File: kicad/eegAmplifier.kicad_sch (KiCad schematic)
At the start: 28 parts

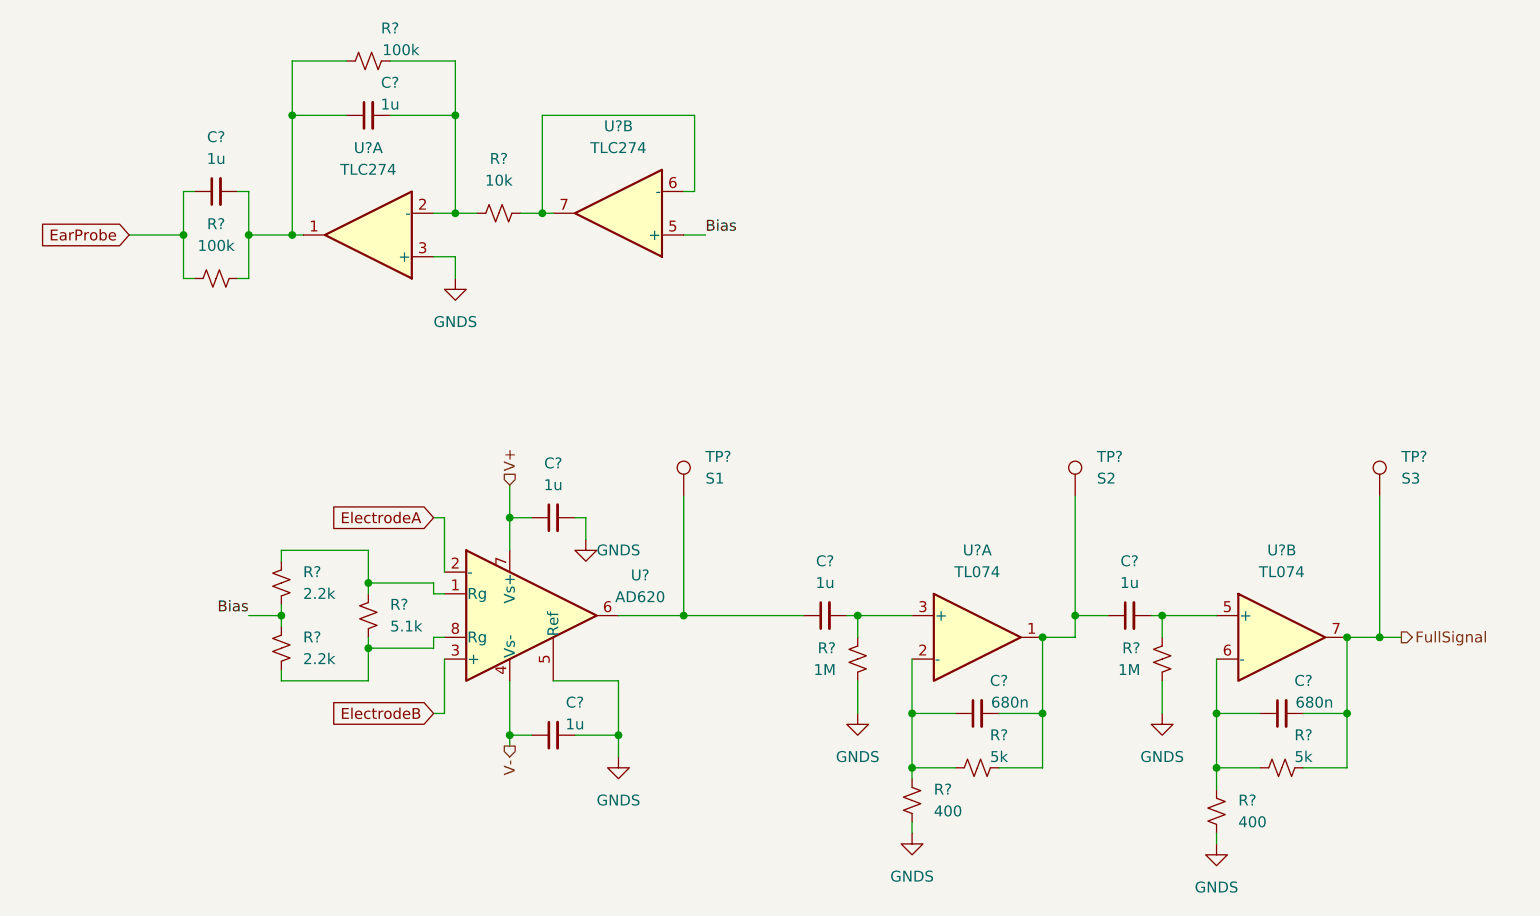
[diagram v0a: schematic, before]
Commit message: Added charge pump to generate rails, switch
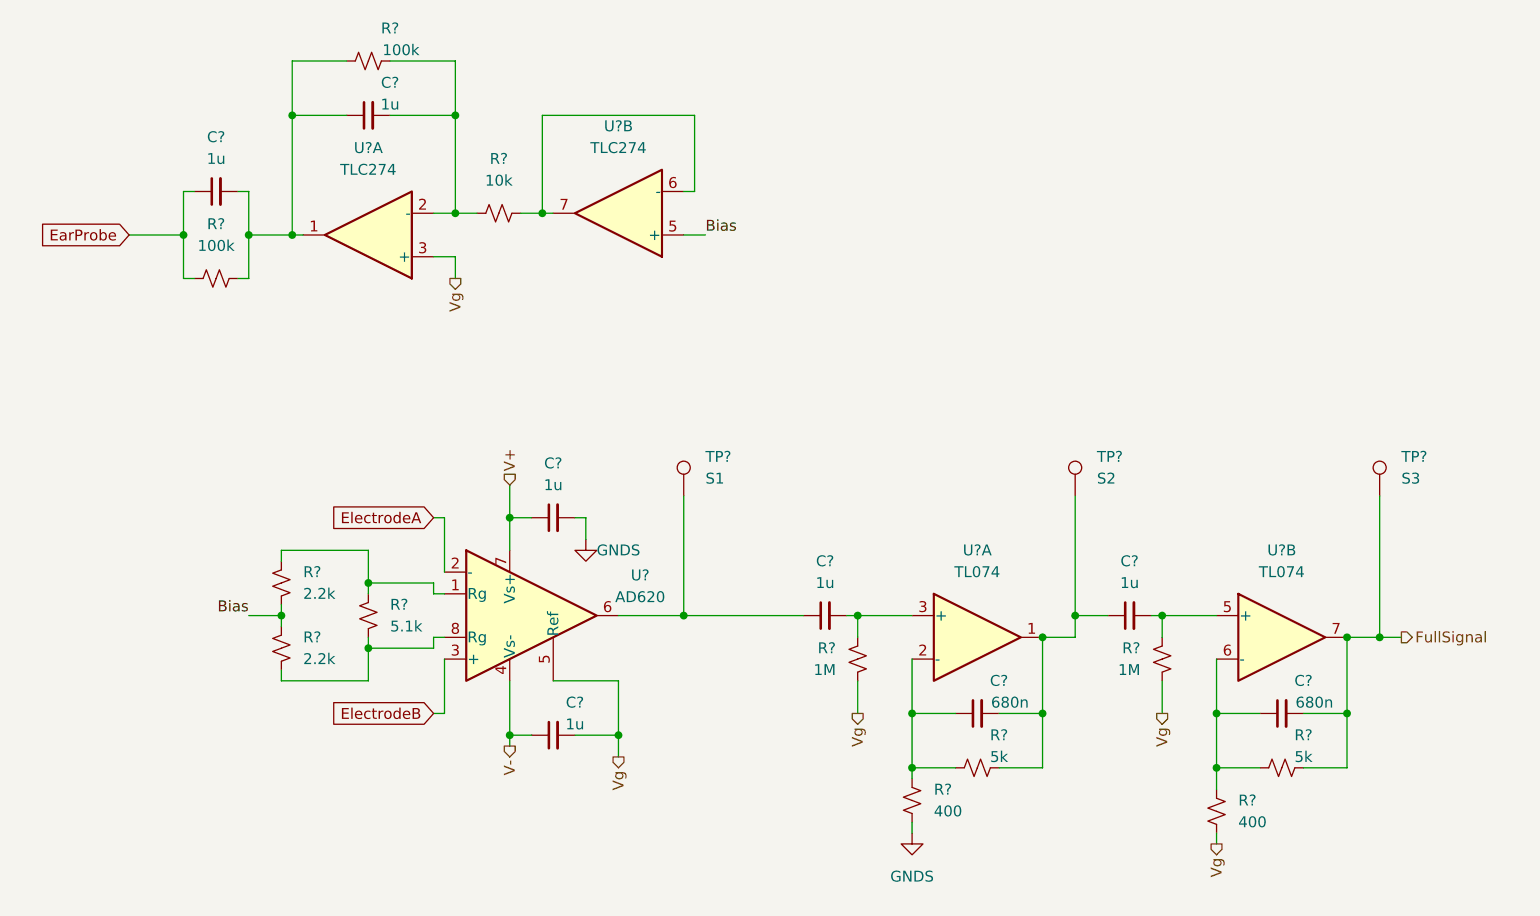
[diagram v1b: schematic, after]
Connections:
- net GNDS: no longer C?.2, R?.1, R?.1, R?.2, U?.3 (+), U?.5 (Ref)
- new net Vg: C?.2, R?.1, R?.1, R?.2, U?.3 (+), U?.5 (Ref)
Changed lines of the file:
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@@
     )
+  )
+  (hierarchical_label "Vg" (shape output) (at 195.58 132.08 270)
+    (effects (font (size 1.27 1.27)) (justify right))
+  )
+  (hierarchical_label "Vg" (shape output) (at 160.02 132.08 270)
+    (effects (font (size 1.27 1.27)) (justify right))
+  )
+  (hierarchical_label "Vg" (shape output) (at 113.03 81.28 270)
+    (effects (font (size 1.27 1.27)) (justify right))
   )
   (hierarchical_label "V-" (shape output) (at 119.38 135.89 270)
+    (effects (font (size 1.27 1.27)) (justify right))
+  )
+  (hierarchical_label "Vg" (shape output) (at 201.93 147.32 270)
+    (effects (font (size 1.27 1.27)) (justify right))
+  )
+  (hierarchical_label "Vg" (shape output) (at 132.08 137.16 270)
     (effects (font (size 1.27 1.27)) (justify right))
   )
@@
     (pin "2")
   )
-  (symbol (lib_id "power:GNDS") (at 113.03 81.28 0) (unit 1)
-    (in_bom yes) (on_board yes) (fields_autoplaced)
-    (property "Reference" "#PWR?" (id 0) (at 113.03 87.63 0)
-      (effects (font (size 1.27 1.27)) hide)
-    )
-    (property "Value" "GNDS" (id 1) (at 113.03 86.36 0))
-    (property "Footprint" "" (id 2) (at 113.03 81.28 0)
-      (effects (font (size 1.27 1.27)) hide)
-    )
-    (property "Datasheet" "" (id 3) (at 113.03 81.28 0)
-      (effects (font (size 1.27 1.27)) hide)
-    )
-    (pin "1")
-  )
-  (symbol (lib_id "power:GNDS") (at 201.93 147.32 0) (unit 1)
-    (in_bom yes) (on_board yes) (fields_autoplaced)
-    (property "Reference" "#PWR?" (id 0) (at 201.93 153.67 0)
-      (effects (font (size 1.27 1.27)) hide)
-    )
-    (property "Value" "GNDS" (id 1) (at 201.93 152.4 0))
-    (property "Footprint" "" (id 2) (at 201.93 147.32 0)
-      (effects (font (size 1.27 1.27)) hide)
-    )
-    (property "Datasheet" "" (id 3) (at 201.93 147.32 0)
-      (effects (font (size 1.27 1.27)) hide)
-    )
-    (pin "1")
-  )
   (symbol (lib_id "Device:C_Small") (at 191.77 120.65 90) (unit 1)
     (in_bom yes) (on_board yes) (fields_autoplaced)
@@
     (pin "3")
   )
-  (symbol (lib_id "power:GNDS") (at 132.08 137.16 0) (unit 1)
-    (in_bom yes) (on_board yes) (fields_autoplaced)
-    (property "Reference" "#PWR?" (id 0) (at 132.08 143.51 0)
-      (effects (font (size 1.27 1.27)) hide)
-    )
-    (property "Value" "GNDS" (id 1) (at 132.08 142.24 0))
-    (property "Footprint" "" (id 2) (at 132.08 137.16 0)
-      (effects (font (size 1.27 1.27)) hide)
-    )
-    (property "Datasheet" "" (id 3) (at 132.08 137.16 0)
-      (effects (font (size 1.27 1.27)) hide)
-    )
-    (pin "1")
-  )
   (symbol (lib_id "Device:R_Small_US") (at 102.87 55.88 90) (unit 1)
     (in_bom yes) (on_board yes)
@@
     (pin "1")
     (pin "2")
-  )
-  (symbol (lib_id "power:GNDS") (at 195.58 132.08 0) (unit 1)
-    (in_bom yes) (on_board yes) (fields_autoplaced)
-    (property "Reference" "#PWR?" (id 0) (at 195.58 138.43 0)
-      (effects (font (size 1.27 1.27)) hide)
-    )
-    (property "Value" "GNDS" (id 1) (at 195.58 137.16 0))
-    (property "Footprint" "" (id 2) (at 195.58 132.08 0)
-      (effects (font (size 1.27 1.27)) hide)
-    )
-    (property "Datasheet" "" (id 3) (at 195.58 132.08 0)
-      (effects (font (size 1.27 1.27)) hide)
-    )
-    (pin "1")
   )
   (symbol (lib_id "Device:R_Small_US") (at 92.71 116.84 0) (mirror y) (unit 1)
@@
     (pin "2")
   )
-  (symbol (lib_id "power:GNDS") (at 160.02 132.08 0) (unit 1)
-    (in_bom yes) (on_board yes) (fields_autoplaced)
-    (property "Reference" "#PWR?" (id 0) (at 160.02 138.43 0)
-      (effects (font (size 1.27 1.27)) hide)
-    )
-    (property "Value" "GNDS" (id 1) (at 160.02 137.16 0))
-    (property "Footprint" "" (id 2) (at 160.02 132.08 0)
-      (effects (font (size 1.27 1.27)) hide)
-    )
-    (property "Datasheet" "" (id 3) (at 160.02 132.08 0)
-      (effects (font (size 1.27 1.27)) hide)
-    )
-    (pin "1")
-  )
   (symbol (lib_id "Device:C_Small") (at 124.46 109.22 90) (unit 1)

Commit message: Pin assignment, electrode headers
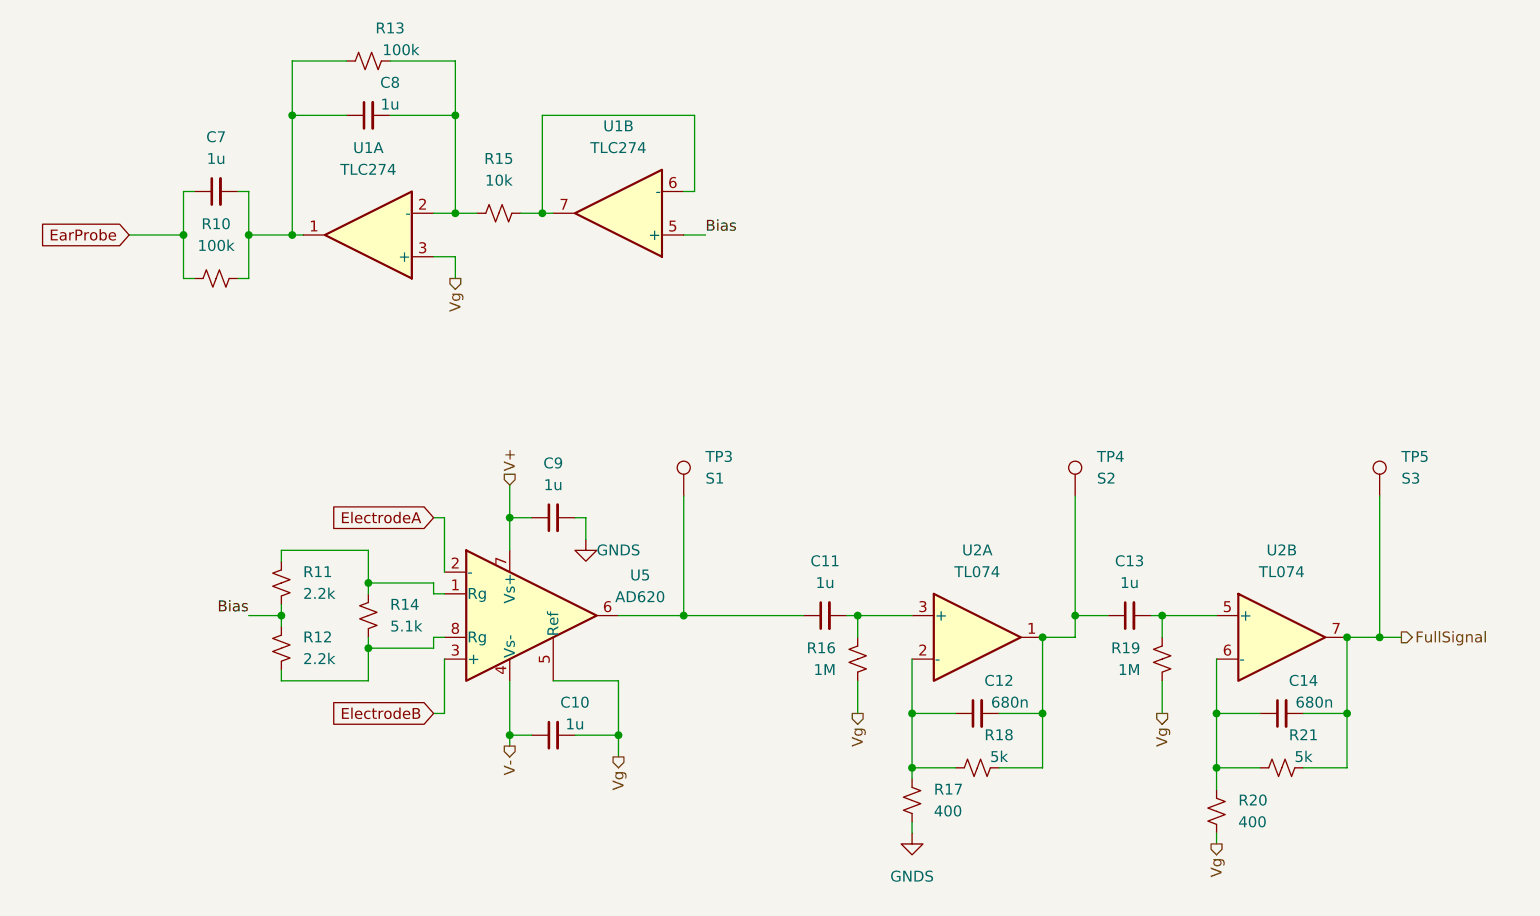
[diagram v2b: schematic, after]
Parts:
- gave numbers to parts that had none: 26

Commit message: Done footprint assignment
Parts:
- C10, C11, C13, C7, C8, C9: footprint (none) -> Capacitor_SMD:C_0805_2012Metric_Pad1.18x1.45mm_HandSolder
- C12, C14: footprint (none) -> Capacitor_THT:C_Disc_D3.8mm_W2.6mm_P2.50mm
- R10, R11, R12, R13, R14, R15, R16, R17, R18, R19, R20, R21: footprint (none) -> Resistor_SMD:R_1206_3216Metric_Pad1.30x1.75mm_HandSolder
- TP3, TP4, TP5: footprint (none) -> TestPoint:TestPoint_Pad_D1.0mm
- U1, U2: footprint (none) -> Package_DIP:DIP-14_W7.62mm_LongPads
- U5: footprint (none) -> Package_DIP:DIP-8_W7.62mm_LongPads
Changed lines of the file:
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@@
     (property "Reference" "R21" (id 0) (at 212.09 134.62 90))
     (property "Value" "5k" (id 1) (at 212.09 137.16 90))
-    (property "Footprint" "" (id 2) (at 209.55 138.43 0)
+    (property "Footprint" "Resistor_SMD:R_1206_3216Metric_Pad1.30x1.75mm_HandSolder" (id 2) (at 209.55 138.43 0)
       (effects (font (size 1.27 1.27)) hide)
     )
@@
     (property "Reference" "C7" (id 0) (at 85.0963 64.77 90))
     (property "Value" "1u" (id 1) (at 85.0963 67.31 90))
-    (property "Footprint" "" (id 2) (at 85.09 71.12 0)
+    (property "Footprint" "Capacitor_SMD:C_0805_2012Metric_Pad1.18x1.45mm_HandSolder" (id 2) (at 85.09 71.12 0)
       (effects (font (size 1.27 1.27)) hide)
     )
@@
       (effects (font (size 1.27 1.27)) (justify right))
     )
-    (property "Footprint" "" (id 2) (at 102.87 120.65 0)
+    (property "Footprint" "Resistor_SMD:R_1206_3216Metric_Pad1.30x1.75mm_HandSolder" (id 2) (at 102.87 120.65 0)
       (effects (font (size 1.27 1.27)) hide)
     )
@@
     (property "Reference" "C13" (id 0) (at 191.7763 114.3 90))
     (property "Value" "1u" (id 1) (at 191.7763 116.84 90))
-    (property "Footprint" "" (id 2) (at 191.77 120.65 0)
+    (property "Footprint" "Capacitor_SMD:C_0805_2012Metric_Pad1.18x1.45mm_HandSolder" (id 2) (at 191.77 120.65 0)
       (effects (font (size 1.27 1.27)) hide)
     )
@@
       (effects (font (size 1.27 1.27)) (justify left))
     )
-    (property "Footprint" "" (id 2) (at 190.5 106.68 0)
+    (property "Footprint" "TestPoint:TestPoint_Pad_D1.0mm" (id 2) (at 190.5 106.68 0)
       (effects (font (size 1.27 1.27)) hide)
     )
@@
       (effects (font (size 1.27 1.27)) (justify left))
     )
-    (property "Footprint" "" (id 2) (at 166.37 142.24 0)
+    (property "Footprint" "Resistor_SMD:R_1206_3216Metric_Pad1.30x1.75mm_HandSolder" (id 2) (at 166.37 142.24 0)
       (effects (font (size 1.27 1.27)) hide)
     )
@@
     (property "Reference" "C14" (id 0) (at 212.09 128.27 90))
     (property "Value" "680n" (id 1) (at 213.36 130.81 90))
-    (property "Footprint" "" (id 2) (at 209.55 132.08 0)
+    (property "Footprint" "Capacitor_THT:C_Disc_D3.8mm_W2.6mm_P2.50mm" (id 2) (at 209.55 132.08 0)
       (effects (font (size 1.27 1.27)) hide)
     )
@@
     (property "Reference" "U1" (id 0) (at 102.87 66.04 0))
     (property "Value" "TLC274" (id 1) (at 102.87 68.58 0))
-    (property "Footprint" "" (id 2) (at 104.14 78.74 0)
+    (property "Footprint" "Package_DIP:DIP-14_W7.62mm_LongPads" (id 2) (at 104.14 78.74 0)
       (effects (font (size 1.27 1.27)) hide)
     )
@@
     (property "Reference" "R13" (id 0) (at 105.41 52.07 90))
     (property "Value" "100k" (id 1) (at 106.68 54.61 90))
-    (property "Footprint" "" (id 2) (at 102.87 55.88 0)
+    (property "Footprint" "Resistor_SMD:R_1206_3216Metric_Pad1.30x1.75mm_HandSolder" (id 2) (at 102.87 55.88 0)
       (effects (font (size 1.27 1.27)) hide)
     )
@@
     (property "Reference" "C8" (id 0) (at 105.41 58.42 90))
     (property "Value" "1u" (id 1) (at 105.41 60.96 90))
-    (property "Footprint" "" (id 2) (at 102.87 62.23 0)
+    (property "Footprint" "Capacitor_SMD:C_0805_2012Metric_Pad1.18x1.45mm_HandSolder" (id 2) (at 102.87 62.23 0)
       (effects (font (size 1.27 1.27)) hide)
     )
@@
     (property "Reference" "U2" (id 0) (at 209.55 113.03 0))
     (property "Value" "TL074" (id 1) (at 209.55 115.57 0))
-    (property "Footprint" "" (id 2) (at 208.28 120.65 0)
+    (property "Footprint" "Package_DIP:DIP-14_W7.62mm_LongPads" (id 2) (at 208.28 120.65 0)
       (effects (font (size 1.27 1.27)) hide)
     )
@@
     (property "Reference" "C11" (id 0) (at 156.2163 114.3 90))
     (property "Value" "1u" (id 1) (at 156.2163 116.84 90))
-    (property "Footprint" "" (id 2) (at 156.21 120.65 0)
+    (property "Footprint" "Capacitor_SMD:C_0805_2012Metric_Pad1.18x1.45mm_HandSolder" (id 2) (at 156.21 120.65 0)
       (effects (font (size 1.27 1.27)) hide)
     )
@@
       (effects (font (size 1.27 1.27)) (justify right))
     )
-    (property "Footprint" "" (id 2) (at 92.71 116.84 0)
+    (property "Footprint" "Resistor_SMD:R_1206_3216Metric_Pad1.30x1.75mm_HandSolder" (id 2) (at 92.71 116.84 0)
       (effects (font (size 1.27 1.27)) hide)
     )
@@
     (property "Reference" "U1" (id 0) (at 132.08 63.5 0))
     (property "Value" "TLC274" (id 1) (at 132.08 66.04 0))
-    (property "Footprint" "" (id 2) (at 133.35 76.2 0)
+    (property "Footprint" "Package_DIP:DIP-14_W7.62mm_LongPads" (id 2) (at 133.35 76.2 0)
       (effects (font (size 1.27 1.27)) hide)
     )
@@
     (property "Reference" "C12" (id 0) (at 176.53 128.27 90))
     (property "Value" "680n" (id 1) (at 177.8 130.81 90))
-    (property "Footprint" "" (id 2) (at 173.99 132.08 0)
+    (property "Footprint" "Capacitor_THT:C_Disc_D3.8mm_W2.6mm_P2.50mm" (id 2) (at 173.99 132.08 0)
       (effects (font (size 1.27 1.27)) hide)
     )
@@
       (effects (font (size 1.27 1.27)) (justify right))
     )
-    (property "Footprint" "" (id 2) (at 195.58 125.73 0)
+    (property "Footprint" "Resistor_SMD:R_1206_3216Metric_Pad1.30x1.75mm_HandSolder" (id 2) (at 195.58 125.73 0)
       (effects (font (size 1.27 1.27)) hide)
     )
@@
     (property "Reference" "U5" (id 0) (at 134.62 115.951 0))
     (property "Value" "AD620" (id 1) (at 134.62 118.491 0))
-    (property "Footprint" "" (id 2) (at 121.92 120.65 0)
+    (property "Footprint" "Package_DIP:DIP-8_W7.62mm_LongPads" (id 2) (at 121.92 120.65 0)
       (effects (font (size 1.27 1.27)) hide)
     )
@@
       (effects (font (size 1.27 1.27)) (justify left))
     )
-    (property "Footprint" "" (id 2) (at 201.93 143.51 0)
+    (property "Footprint" "Resistor_SMD:R_1206_3216Metric_Pad1.30x1.75mm_HandSolder" (id 2) (at 201.93 143.51 0)
       (effects (font (size 1.27 1.27)) hide)
     )
@@
     (property "Reference" "U2" (id 0) (at 173.99 113.03 0))
     (property "Value" "TL074" (id 1) (at 173.99 115.57 0))
-    (property "Footprint" "" (id 2) (at 172.72 120.65 0)
+    (property "Footprint" "Package_DIP:DIP-14_W7.62mm_LongPads" (id 2) (at 172.72 120.65 0)
       (effects (font (size 1.27 1.27)) hide)
     )
@@
       (effects (font (size 1.27 1.27)) (justify left))
     )
-    (property "Footprint" "" (id 2) (at 226.06 106.68 0)
+    (property "Footprint" "TestPoint:TestPoint_Pad_D1.0mm" (id 2) (at 226.06 106.68 0)
       (effects (font (size 1.27 1.27)) hide)
     )
@@
       (effects (font (size 1.27 1.27)) (justify right))
     )
-    (property "Footprint" "" (id 2) (at 92.71 124.46 0)
+    (property "Footprint" "Resistor_SMD:R_1206_3216Metric_Pad1.30x1.75mm_HandSolder" (id 2) (at 92.71 124.46 0)
       (effects (font (size 1.27 1.27)) hide)
     )
@@
     (property "Reference" "R15" (id 0) (at 118.11 67.31 90))
     (property "Value" "10k" (id 1) (at 118.11 69.85 90))
-    (property "Footprint" "" (id 2) (at 118.11 73.66 0)
+    (property "Footprint" "Resistor_SMD:R_1206_3216Metric_Pad1.30x1.75mm_HandSolder" (id 2) (at 118.11 73.66 0)
       (effects (font (size 1.27 1.27)) hide)
     )
@@
     (property "Reference" "R10" (id 0) (at 85.09 74.93 90))
     (property "Value" "100k" (id 1) (at 85.09 77.47 90))
-    (property "Footprint" "" (id 2) (at 85.09 81.28 0)
+    (property "Footprint" "Resistor_SMD:R_1206_3216Metric_Pad1.30x1.75mm_HandSolder" (id 2) (at 85.09 81.28 0)
       (effects (font (size 1.27 1.27)) hide)
     )
@@
     (property "Reference" "R18" (id 0) (at 176.53 134.62 90))
     (property "Value" "5k" (id 1) (at 176.53 137.16 90))
-    (property "Footprint" "" (id 2) (at 173.99 138.43 0)
+    (property "Footprint" "Resistor_SMD:R_1206_3216Metric_Pad1.30x1.75mm_HandSolder" (id 2) (at 173.99 138.43 0)
       (effects (font (size 1.27 1.27)) hide)
     )
@@
     (property "Reference" "C10" (id 0) (at 127 130.81 90))
     (property "Value" "1u" (id 1) (at 127 133.35 90))
-    (property "Footprint" "" (id 2) (at 124.46 134.62 0)
+    (property "Footprint" "Capacitor_SMD:C_0805_2012Metric_Pad1.18x1.45mm_HandSolder" (id 2) (at 124.46 134.62 0)
       (effects (font (size 1.27 1.27)) hide)
     )
@@
     (property "Reference" "C9" (id 0) (at 124.4663 102.87 90))
     (property "Value" "1u" (id 1) (at 124.4663 105.41 90))
-    (property "Footprint" "" (id 2) (at 124.46 109.22 0)
+    (property "Footprint" "Capacitor_SMD:C_0805_2012Metric_Pad1.18x1.45mm_HandSolder" (id 2) (at 124.46 109.22 0)
       (effects (font (size 1.27 1.27)) hide)
     )
@@
       (effects (font (size 1.27 1.27)) (justify right))
     )
-    (property "Footprint" "" (id 2) (at 160.02 125.73 0)
+    (property "Footprint" "Resistor_SMD:R_1206_3216Metric_Pad1.30x1.75mm_HandSolder" (id 2) (at 160.02 125.73 0)
       (effects (font (size 1.27 1.27)) hide)
     )
@@
       (effects (font (size 1.27 1.27)) (justify left))
     )
-    (property "Footprint" "" (id 2) (at 144.78 106.68 0)
-      (effects (font (size 1.27 1.27)) hide)
-    )
+    (property "Footprint" "TestPoint:TestPoint_Pad_D1.0mm" (id 2) (at 144.78 106.68 0)
+      (effects (font (size 1.27 1.27)) hide)
+    )
